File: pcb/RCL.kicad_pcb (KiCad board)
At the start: 2 copper layers, 52 x 52 mm, 86 parts, among them J1 USB_C_Receptacle, J2 Conn_01x02_Pin, J3 Conn_01x05_Pin, Q1 BSP613, Q2 AO3416A, Q3 AO3416A, Q4 AO3416A, SW1 SW_SPDT, SW2 SW_DIP_x02, SW3 SW_Push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

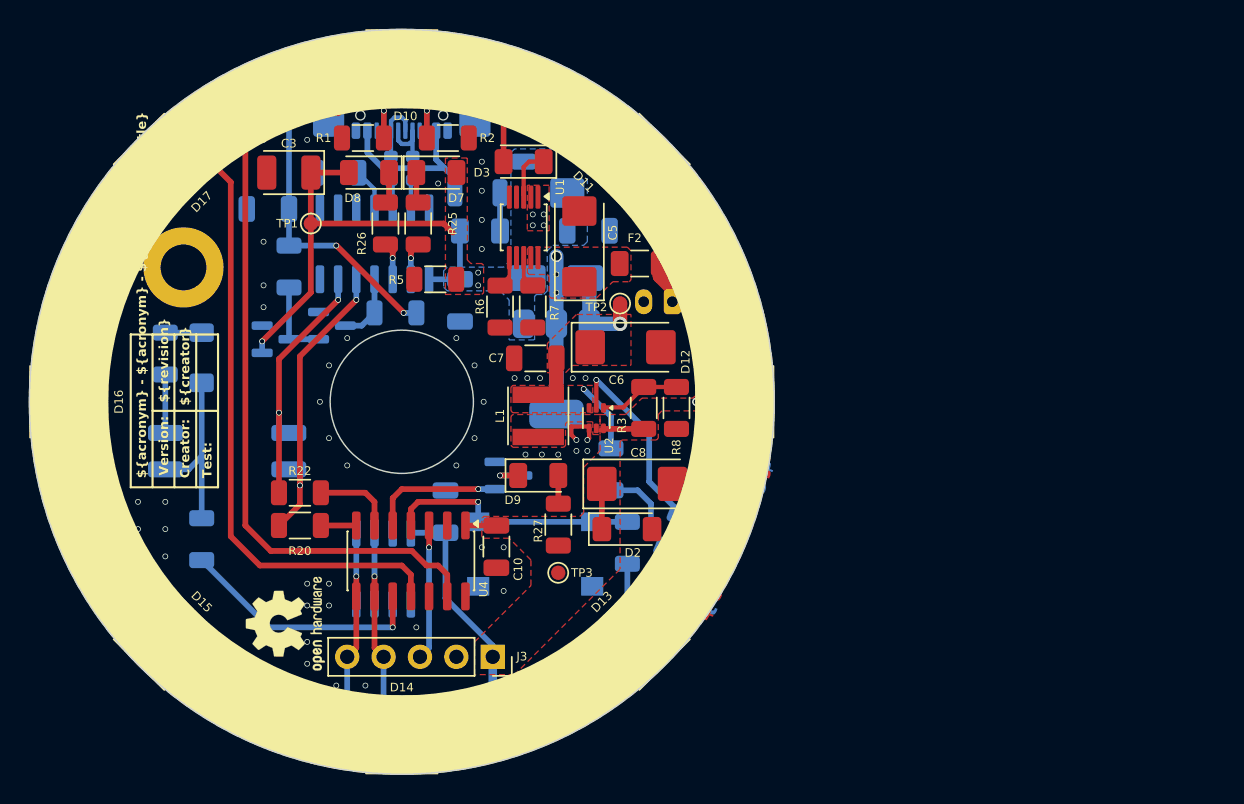
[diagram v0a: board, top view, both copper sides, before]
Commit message: Move pcb position on sheet
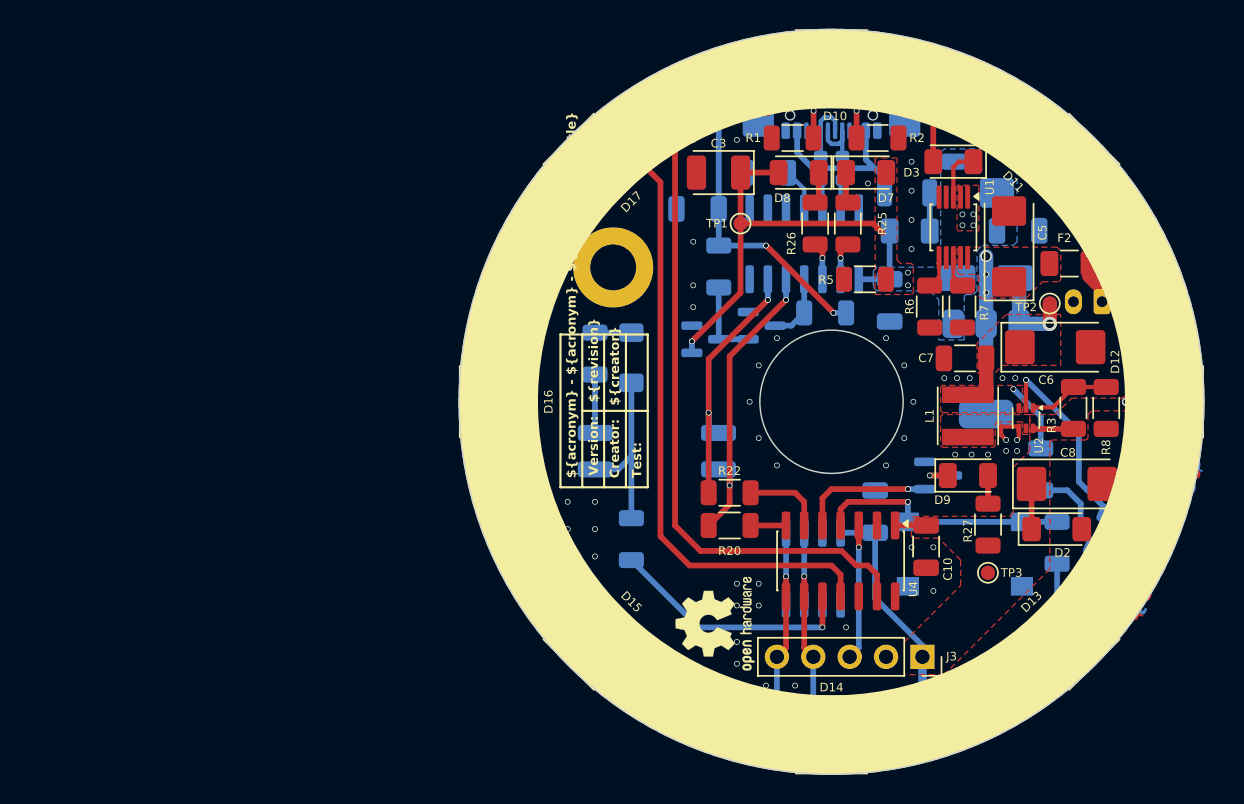
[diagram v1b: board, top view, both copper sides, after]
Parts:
- moved C11 30.0 mm to (147.7, 74.8)
- moved R15 30.0 mm to (140.5, 84.9)
- moved C1 30.0 mm to (168.6, 71.2)
- moved C12 30.0 mm to (152.5, 72.3)
- moved C15 30.0 mm to (181.1, 89.7)
- moved C16 30.0 mm to (169.9, 106.9)
- moved C19 30.0 mm to (134.4, 88.3)
- moved C2 30.0 mm to (170.0, 76.3)
- moved C4 30.0 mm to (161.1, 81.2)
- moved C5 30.0 mm to (169.4, 77.4)
- moved C6 30.0 mm to (172.6, 84.5)
- moved C7 30.0 mm to (166.3, 85.2)
- moved C8 30.0 mm to (173.4, 94.0)
- moved C9 30.0 mm to (160.0, 95.9)
- moved D1 30.0 mm to (167.8, 79.6)
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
